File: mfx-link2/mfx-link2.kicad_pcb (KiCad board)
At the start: 2 copper layers, 50 x 50 mm, 58 parts, among them P1 CONN_01X04, P2 Gleisbox, P4 UART, P5 I2C, P6 CONN_02X03, P7 POTI, P8 IBT-2, Q1 BC817-40, SW1 SW_PUSH, T1 53040C, U1 6N137, U2 7805, U3 LM393, U4 78L05, U5 PIC16F1709

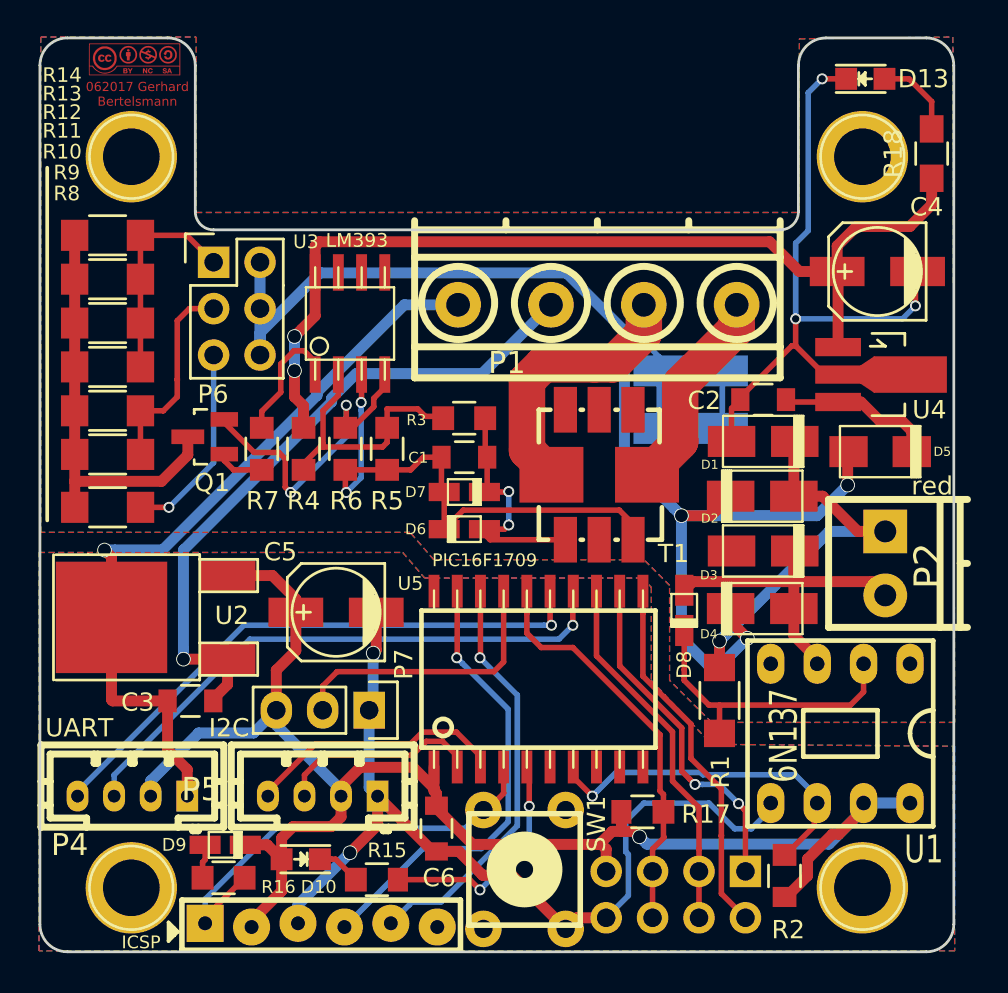
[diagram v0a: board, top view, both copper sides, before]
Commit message: use right Grove I2C mapping
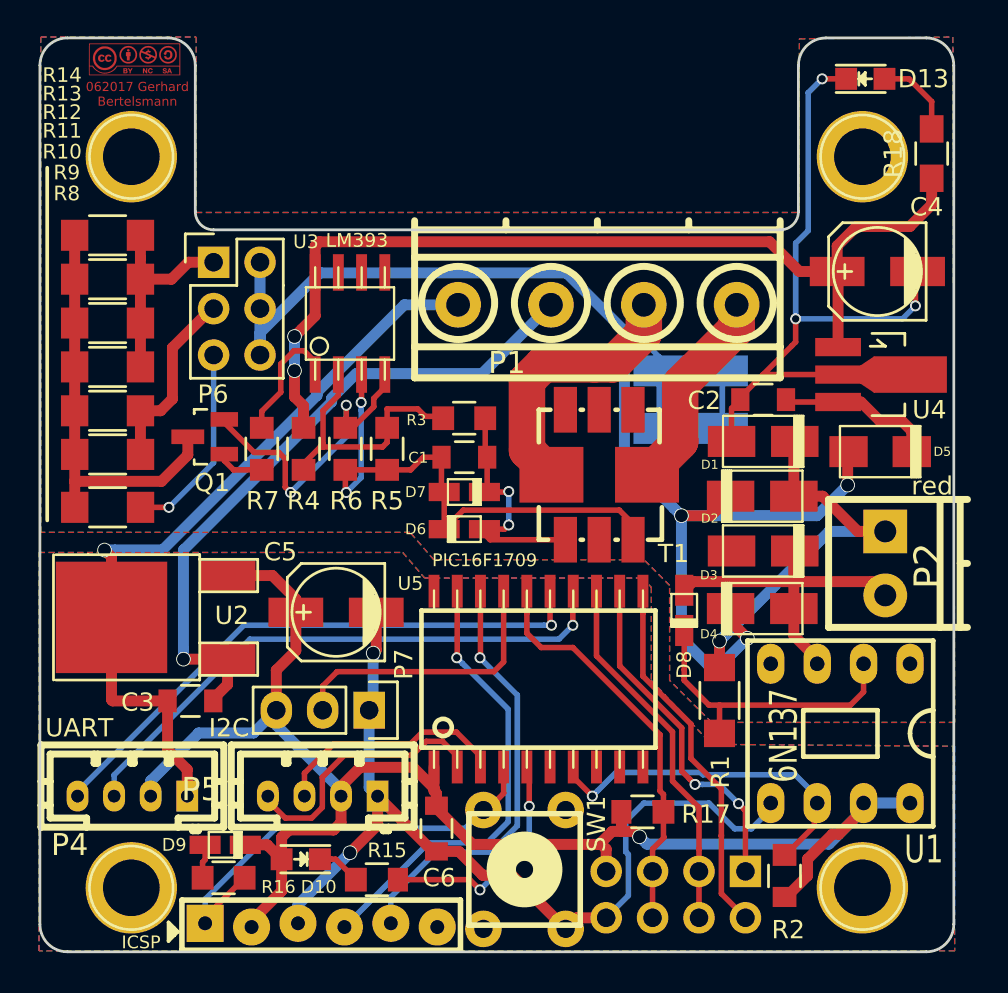
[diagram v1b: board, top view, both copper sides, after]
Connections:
- P5 pad 3: /SCL -> /SDA
- P5 pad 4: /SDA -> /SCL
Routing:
- net /SCL: track 11.2 -> 14.6 mm
- net GNDA: track 52.7 -> 54.5 mm
- net /SDA: track 14.4 -> 13.0 mm
- net Net-(P6-Pad3): track 11.3 -> 10.5 mm
- net /PGC: track 22.8 -> 23.7 mm

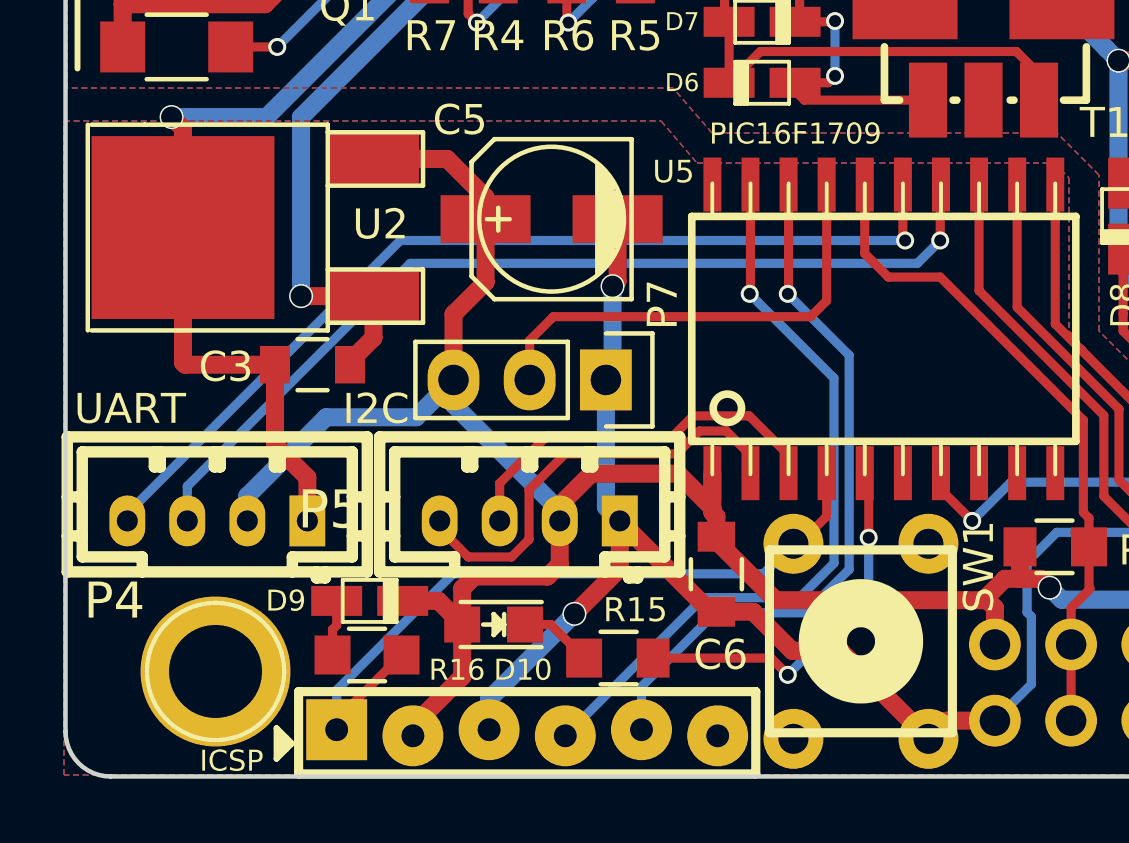
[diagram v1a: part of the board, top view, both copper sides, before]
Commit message: move grove connectors
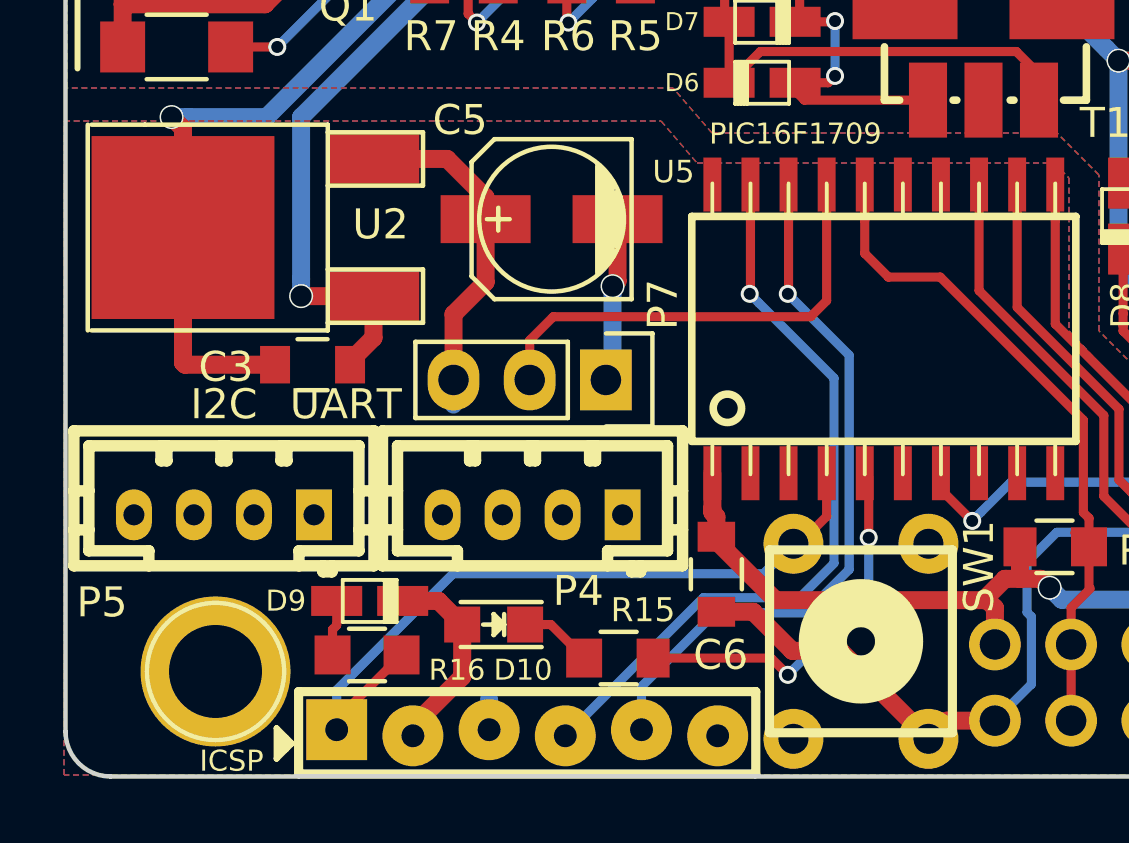
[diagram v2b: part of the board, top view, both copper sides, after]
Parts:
- moved P4 10.5 mm to (136.0, 135.1)
- moved P5 10.2 mm to (125.7, 135.1)
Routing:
- net /RxD: track 31.8 -> 0.00 mm, vias 1 -> 0
- net /TxD: track 31.5 -> 0.04 mm, vias 1 -> 0
- net VCC: track 87.1 -> 59.7 mm
- net GND: track 92.6 -> 70.0 mm, vias 3 -> 2
- net /SCL: track 14.6 -> 0.60 mm
- net /SDA: track 13.0 -> 0.60 mm

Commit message: wip
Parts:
- added R20: 3k3, Resistors_SMD:R_0805_HandSolderingII, F.Cu at (122.6, 131.1)
- added R21: 3k3, Resistors_SMD:R_0805_HandSolderingII, F.Cu at (127.0, 131.1)
- C4, C5: value 47uF -> 10uF
- moved C3 2.34 mm to (131.0, 129.8)
- moved P7 1.34 mm to (139.8, 130.5)
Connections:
- U3 pad 5: (no net) -> GNDA
- U3 pad 6: (no net) -> GNDA
- U3 pad 7: (no net) -> Net-(U3-Pad7)
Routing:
- net VCC: track 59.7 -> 90.9 mm
- net GND: track 70.0 -> 59.2 mm
- net /SCL: track 0.60 -> 5.16 mm
- net /SDA: track 0.60 -> 5.09 mm
- net Net-(P7-Pad2): track 15.6 -> 14.4 mm

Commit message: wip
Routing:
- net GND: track 59.2 -> 99.7 mm
- net /SCL: track 5.16 -> 31.0 mm
- net /SDA: track 5.09 -> 28.9 mm
- net /RxD: track 0.00 -> 21.8 mm, vias 0 -> 2
- net /TxD: track 0.04 -> 21.6 mm, vias 0 -> 2
- net VCC: track 90.9 -> 95.2 mm
- net /PGC: track 23.7 -> 22.8 mm
- net Net-(P7-Pad2): track 14.4 -> 13.7 mm

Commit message: go for last QS
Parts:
- moved R18 1.02 mm to (169.2, 101.2)
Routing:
- net Net-(D13-Pad2): track 4.59 -> 5.59 mm
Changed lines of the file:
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@@
-(kicad_pcb (version 4) (host pcbnew 4.0.1-stable)
+(kicad_pcb (version 4) (host pcbnew 4.0.2+dfsg1-stable)
   (general
     (links 120)
     (no_connects 0)
-    (area 102.300001 82.5 173.904 144.373)
+    (area 120.374999 93.774999 170.525001 143.925001)
     (thickness 1.6)
     (drawings 29)
@@
     (descr "SMT capacitor, aluminium electrolytic, 5x5.3")
     (attr smd)
-    (fp_text reference C4 (at -2.6924 3.5306 180) (layer F.SilkS)
+    (fp_text reference C4 (at 4.0684 1.7292 180) (layer F.SilkS)
       (effects (font (size 1 1) (thickness 0.15)))
     )
@@
   )
   (module Resistors_SMD:R_0805_HandSoldering (layer F.Cu)
-    (at 169.2402 100.1776 90)
+    (at 169.2 101.2 90)
     (descr "Resistor SMD 0805, hand soldering")
     (tags "resistor 0805")
@@
   (segment (start 123.985 121.869) (end 124.366 122.25) (width 0.6) (layer F.Cu) (net 4))
   (via (at 123.985 121.869) (size 0.8) (drill 0.7) (layers F.Cu B.Cu) (net 4))
-  (segment (start 168.0464 104.1654) (end 169.2402 102.9716) (width 0.6) (layer F.Cu) (net 5))
-  (segment (start 169.2402 102.9716) (end 169.2402 101.5276) (width 0.6) (layer F.Cu) (net 5))
-  (segment (start 165.13246 104.1654) (end 168.0464 104.1654) (width 0.6) (layer F.Cu) (net 5))
-  (segment (start 164.06876 106.6292) (end 164.06876 105.2291) (width 0.6) (layer F.Cu) (net 5))
-  (segment (start 164.06876 105.2291) (end 165.13246 104.1654) (width 0.6) (layer F.Cu) (net 5))
+  (segment (start 164.06876 106.6292) (end 164.06876 104.93124) (width 0.6) (layer F.Cu) (net 5))
+  (segment (start 169.2 104) (end 169.2 102.55) (width 0.6) (layer F.Cu) (net 5))
+  (segment (start 168.7 104.5) (end 169.2 104) (width 0.6) (layer F.Cu) (net 5))
+  (segment (start 164.5 104.5) (end 168.7 104.5) (width 0.6) (layer F.Cu) (net 5))
+  (segment (start 164.06876 104.93124) (end 164.5 104.5) (width 0.6) (layer F.Cu) (net 5))
   (segment (start 134.378719 112.056886) (end 134.378703 112.056902) (width 0.6) (layer B.Cu) (net 5))
   (segment (start 134.378703 113.486703) (end 134.378703 112.056902) (width 0.6) (layer F.Cu) (net 5))
@@
   (segment (start 151.791 111.709) (end 153.49 110.01) (width 2) (layer F.Cu) (net 42))
   (segment (start 147.099 116.414) (end 148.435 117.75) (width 2) (layer F.Cu) (net 42))
-  (segment (start 166.65702 96.0882) (end 167.9956 96.0882) (width 0.3048) (layer F.Cu) (net 43))
-  (segment (start 169.2402 97.3328) (end 169.2402 98.8276) (width 0.3048) (layer F.Cu) (net 43))
-  (segment (start 167.9956 96.0882) (end 169.2402 97.3328) (width 0.3048) (layer F.Cu) (net 43))
+  (segment (start 169.2 99.85) (end 169.2 97.3) (width 0.3048) (layer F.Cu) (net 43))
+  (segment (start 167.9882 96.0882) (end 166.65702 96.0882) (width 0.3048) (layer F.Cu) (net 43))
+  (segment (start 169.2 97.3) (end 167.9882 96.0882) (width 0.3048) (layer F.Cu) (net 43))
   (zone (net 3) (net_name GNDA) (layer F.Cu) (hatch edge 0.508)
     (connect_pads (clearance 0.254))

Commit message: go for last QS - part 2
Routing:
- net Net-(P6-Pad3): track 10.5 -> 11.3 mm
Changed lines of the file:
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@@
     (thickness 1.6)
     (drawings 29)
-    (tracks 532)
+    (tracks 534)
     (zones 0)
     (modules 60)
@@
   (segment (start 144.702995 129.233727) (end 143.762171 129.233727) (width 0.3048) (layer F.Cu) (net 14))
   (segment (start 155.992104 134.39117) (end 156.292103 134.691169) (width 0.3048) (layer F.Cu) (net 15))
+  (segment (start 155.714432 134.113498) (end 155.992104 134.39117) (width 0.3048) (layer F.Cu) (net 15))
+  (segment (start 155.714432 131.754102) (end 155.714432 134.113498) (width 0.3048) (layer F.Cu) (net 15))
   (segment (start 152.1714 124.11964) (end 152.1714 128.21107) (width 0.3048) (layer F.Cu) (net 15))
-  (segment (start 155.565433 131.605103) (end 155.565433 133.964499) (width 0.3048) (layer F.Cu) (net 15))
-  (segment (start 152.1714 128.21107) (end 155.565433 131.605103) (width 0.3048) (layer F.Cu) (net 15))
-  (segment (start 155.565433 133.964499) (end 155.992104 134.39117) (width 0.3048) (layer F.Cu) (net 15))
+  (segment (start 152.1714 128.21107) (end 155.714432 131.754102) (width 0.3048) (layer F.Cu) (net 15))
   (segment (start 158.673907 135.74558) (end 157.619496 134.691169) (width 0.3048) (layer B.Cu) (net 15))
   (segment (start 156.716367 134.691169) (end 156.292103 134.691169) (width 0.3048) (layer B.Cu) (net 15))
@@
   (segment (start 159.05 139.45) (end 159.05 136.121673) (width 0.3048) (layer F.Cu) (net 15))
   (segment (start 158.973906 136.045579) (end 158.673907 135.74558) (width 0.3048) (layer F.Cu) (net 15))
+  (segment (start 153.4414 128.76716) (end 153.4414 125.32444) (width 0.3048) (layer F.Cu) (net 16))
   (segment (start 157.734 137.5156) (end 157.734 134.935754) (width 0.3048) (layer F.Cu) (net 16))
-  (segment (start 153.4414 128.76716) (end 153.4414 125.32444) (width 0.3048) (layer F.Cu) (net 16))
-  (segment (start 156.070244 133.271998) (end 156.070244 131.396004) (width 0.3048) (layer F.Cu) (net 16))
-  (segment (start 157.734 134.935754) (end 156.070244 133.271998) (width 0.3048) (layer F.Cu) (net 16))
-  (segment (start 156.070244 131.396004) (end 153.4414 128.76716) (width 0.3048) (layer F.Cu) (net 16))
+  (segment (start 157.734 134.935754) (end 156.219242 133.420995) (width 0.3048) (layer F.Cu) (net 16))
+  (segment (start 156.219242 131.545002) (end 153.4414 128.76716) (width 0.3048) (layer F.Cu) (net 16))
+  (segment (start 156.219242 133.420995) (end 156.219242 131.545002) (width 0.3048) (layer F.Cu) (net 16))
   (segment (start 153.4414 125.32444) (end 153.4414 124.11964) (width 0.3048) (layer F.Cu) (net 16))
   (segment (start 159.05 141.99) (end 159.05 141.9812) (width 0.3048) (layer F.Cu) (net 16))
@@
   (segment (start 157.734 140.6652) (end 157.734 137.5156) (width 0.3048) (layer F.Cu) (net 16))
   (segment (start 157.734 137.5156) (end 157.734 137.4648) (width 0.3048) (layer F.Cu) (net 16))
-  (segment (start 155.060622 131.814202) (end 155.060622 134.509312) (width 0.3048) (layer F.Cu) (net 17))
-  (segment (start 155.060622 134.509312) (end 156.51 135.95869) (width 0.3048) (layer F.Cu) (net 17))
-  (segment (start 150.9014 127.65498) (end 155.060622 131.814202) (width 0.3048) (layer F.Cu) (net 17))
+  (segment (start 155.209621 134.658311) (end 156.51 135.95869) (width 0.3048) (layer F.Cu) (net 17))
+  (segment (start 156.51 135.95869) (end 156.51 138.228686) (width 0.3048) (layer F.Cu) (net 17))
   (segment (start 156.51 138.228686) (end 156.51 139.45) (width 0.3048) (layer F.Cu) (net 17))
   (segment (start 150.9014 124.11964) (end 150.9014 127.65498) (width 0.3048) (layer F.Cu) (net 17))
-  (segment (start 156.51 135.95869) (end 156.51 138.228686) (width 0.3048) (layer F.Cu) (net 17))
+  (segment (start 155.209621 131.963201) (end 155.209621 134.658311) (width 0.3048) (layer F.Cu) (net 17))
+  (segment (start 150.9014 127.65498) (end 155.209621 131.963201) (width 0.3048) (layer F.Cu) (net 17))
   (segment (start 156.51 141.99) (end 156.51 139.45) (width 0.3048) (layer F.Cu) (net 17))
+  (segment (start 147.0914 126.4158) (end 147.0914 125.32444) (width 0.3048) (layer F.Cu) (net 18))
   (segment (start 147.0914 125.32444) (end 147.0914 124.11964) (width 0.3048) (layer F.Cu) (net 18))
-  (segment (start 147.0914 126.4158) (end 147.0914 125.32444) (width 0.3048) (layer F.Cu) (net 18))
-  (segment (start 148.970646 127.2032) (end 147.8788 127.2032) (width 0.3048) (layer F.Cu) (net 18))
-  (segment (start 154.378011 135.052011) (end 154.378011 132.610565) (width 0.3048) (layer F.Cu) (net 18))
-  (segment (start 154.378011 132.610565) (end 148.970646 127.2032) (width 0.3048) (layer F.Cu) (net 18))
-  (segment (start 154.566 135.24) (end 154.378011 135.052011) (width 0.3048) (layer F.Cu) (net 18))
+  (segment (start 154.70481 135.10119) (end 154.70481 132.2909) (width 0.3048) (layer F.Cu) (net 18))
+  (segment (start 148.870789 128.195189) (end 147.0914 126.4158) (width 0.3048) (layer F.Cu) (net 18))
+  (segment (start 150.609099 128.195189) (end 148.870789 128.195189) (width 0.3048) (layer F.Cu) (net 18))
+  (segment (start 154.70481 132.2909) (end 150.609099 128.195189) (width 0.3048) (layer F.Cu) (net 18))
   (segment (start 154.566 136.1948) (end 154.566 135.24) (width 0.3048) (layer F.Cu) (net 18))
-  (segment (start 147.8788 127.2032) (end 147.0914 126.4158) (width 0.3048) (layer F.Cu) (net 18))
+  (segment (start 154.566 135.24) (end 154.70481 135.10119) (width 0.3048) (layer F.Cu) (net 18))
   (segment (start 154.566 136.1948) (end 154.093801 135.722601) (width 0.3048) (layer F.Cu) (net 18))
   (segment (start 154.566 137.545086) (end 154.566 136.1948) (width 0.3048) (layer F.Cu) (net 18))
@@
   (segment (start 125.95 107.05) (end 125.95 109.45) (width 0.6) (layer F.Cu) (net 38))
   (segment (start 125.95 109.45) (end 125.95 111.85) (width 0.6) (layer F.Cu) (net 38))
+  (segment (start 129.954 108.661) (end 128.639 108.661) (width 0.6) (layer F.Cu) (net 39))
+  (segment (start 127.05 114.25) (end 125.95 114.25) (width 0.6) (layer F.Cu) (net 39))
+  (segment (start 127.7 113.6) (end 127.05 114.25) (width 0.6) (layer F.Cu) (net 39))
+  (segment (start 127.7 110.8) (end 127.7 113.6) (width 0.6) (layer F.Cu) (net 39))
+  (segment (start 127.7 109.6) (end 127.7 110.8) (width 0.6) (layer F.Cu) (net 39))
+  (segment (start 128.639 108.661) (end 127.7 109.6) (width 0.6) (layer F.Cu) (net 39))
   (segment (start 129.954 108.661) (end 129.839 108.661) (width 0.6) (layer F.Cu) (net 39))
-  (segment (start 129.839 108.661) (end 127.7 110.8) (width 0.6) (layer F.Cu) (net 39))
-  (segment (start 127.7 110.8) (end 127.7 113.6) (width 0.6) (layer F.Cu) (net 39))
-  (segment (start 127.7 113.6) (end 127.05 114.25) (width 0.6) (layer F.Cu) (net 39))
-  (segment (start 127.05 114.25) (end 125.95 114.25) (width 0.6) (layer F.Cu) (net 39))
   (segment (start 125.95 114.25) (end 125.95 116.6316) (width 0.6) (layer F.Cu) (net 39))
   (segment (start 125.95 116.6316) (end 125.9552 116.6368) (width 0.6) (layer F.Cu) (net 39))

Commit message: production
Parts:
- moved D5 0.41 mm to (166.8, 116.5)
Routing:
- net /SDA: track 28.9 -> 30.1 mm
- net /SCL: track 31.0 -> 29.9 mm
- net /PULSE: track 19.6 -> 20.4 mm
- net /VI: track 9.87 -> 10.5 mm

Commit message: wip
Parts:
- added R19: 4k7, Resistors_SMD:R_0805_HandSolderingII, F.Cu at (133.7, 114.2)
- C6: value C -> 100nF
- R4, R6: value 4k7 -> 100k
- moved R4 1.02 mm to (134.9, 117.3)
- moved R7 1.02 mm to (132.6, 117.3)
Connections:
- C2 pad 2: GNDA -> Net-(C2-Pad2)
- C4 pad 2: GNDA -> Net-(C2-Pad2)
- D1 pad 1: GNDA -> Net-(C2-Pad2)
- D13 pad 1: GNDA -> Net-(C2-Pad2)
- D2 pad 1: GNDA -> Net-(C2-Pad2)
- T1 pad 7: Net-(D11-Pad2) -> Net-(T1-Pad7)
- T1 pad 8: Net-(D11-Pad1) -> Net-(T1-Pad8)
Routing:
- net GNDA: track 54.5 -> 4.87 mm, vias 5 -> 0
- net Net-(C2-Pad2): track 0.00 -> 39.8 mm, vias 0 -> 3
- net Net-(T1-Pad8): track 0.00 -> 5.71 mm
- net Net-(D11-Pad1): track 21.8 -> 16.1 mm
- net Net-(D11-Pad2): track 18.4 -> 15.9 mm
- net Net-(T1-Pad7): track 0.00 -> 2.57 mm
- net /_GB_OUT: track 7.05 -> 8.45 mm
- net +5V: track 52.8 -> 53.8 mm
- net Net-(Q1-Pad1): track 2.61 -> 3.46 mm
